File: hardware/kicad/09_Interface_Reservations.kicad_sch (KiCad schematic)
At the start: 27 parts

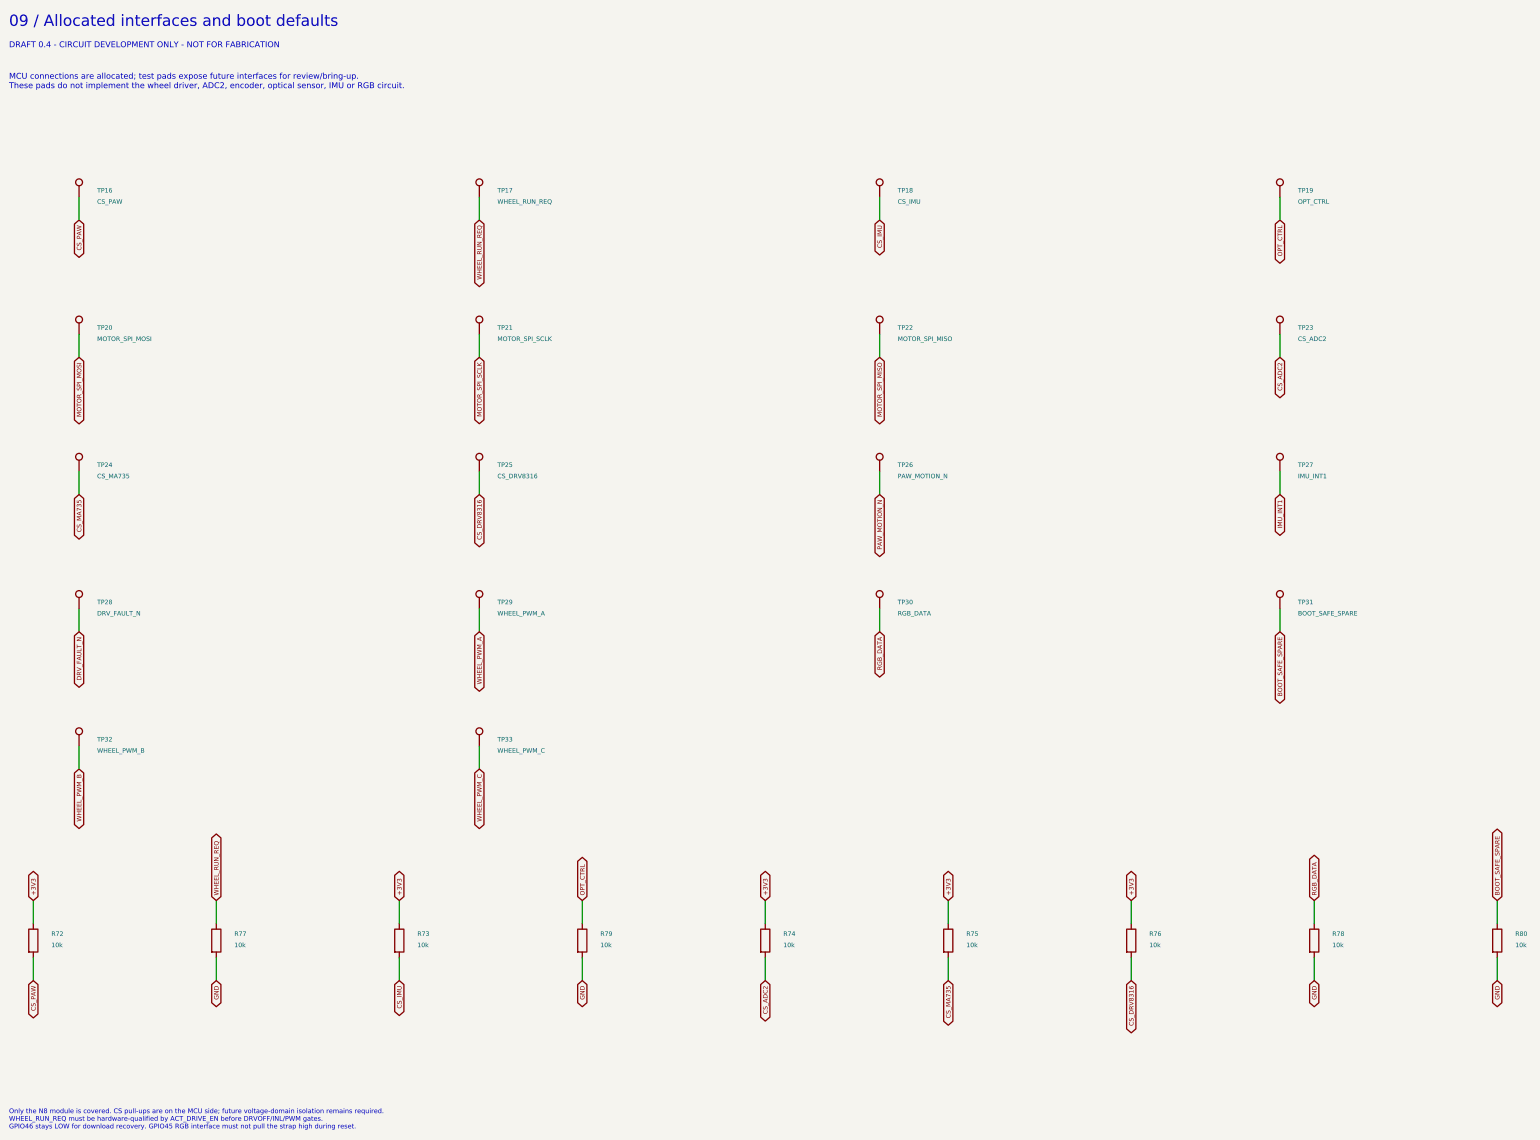
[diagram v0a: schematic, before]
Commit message: Add wheel control circuitry and autonomous regeneration brake
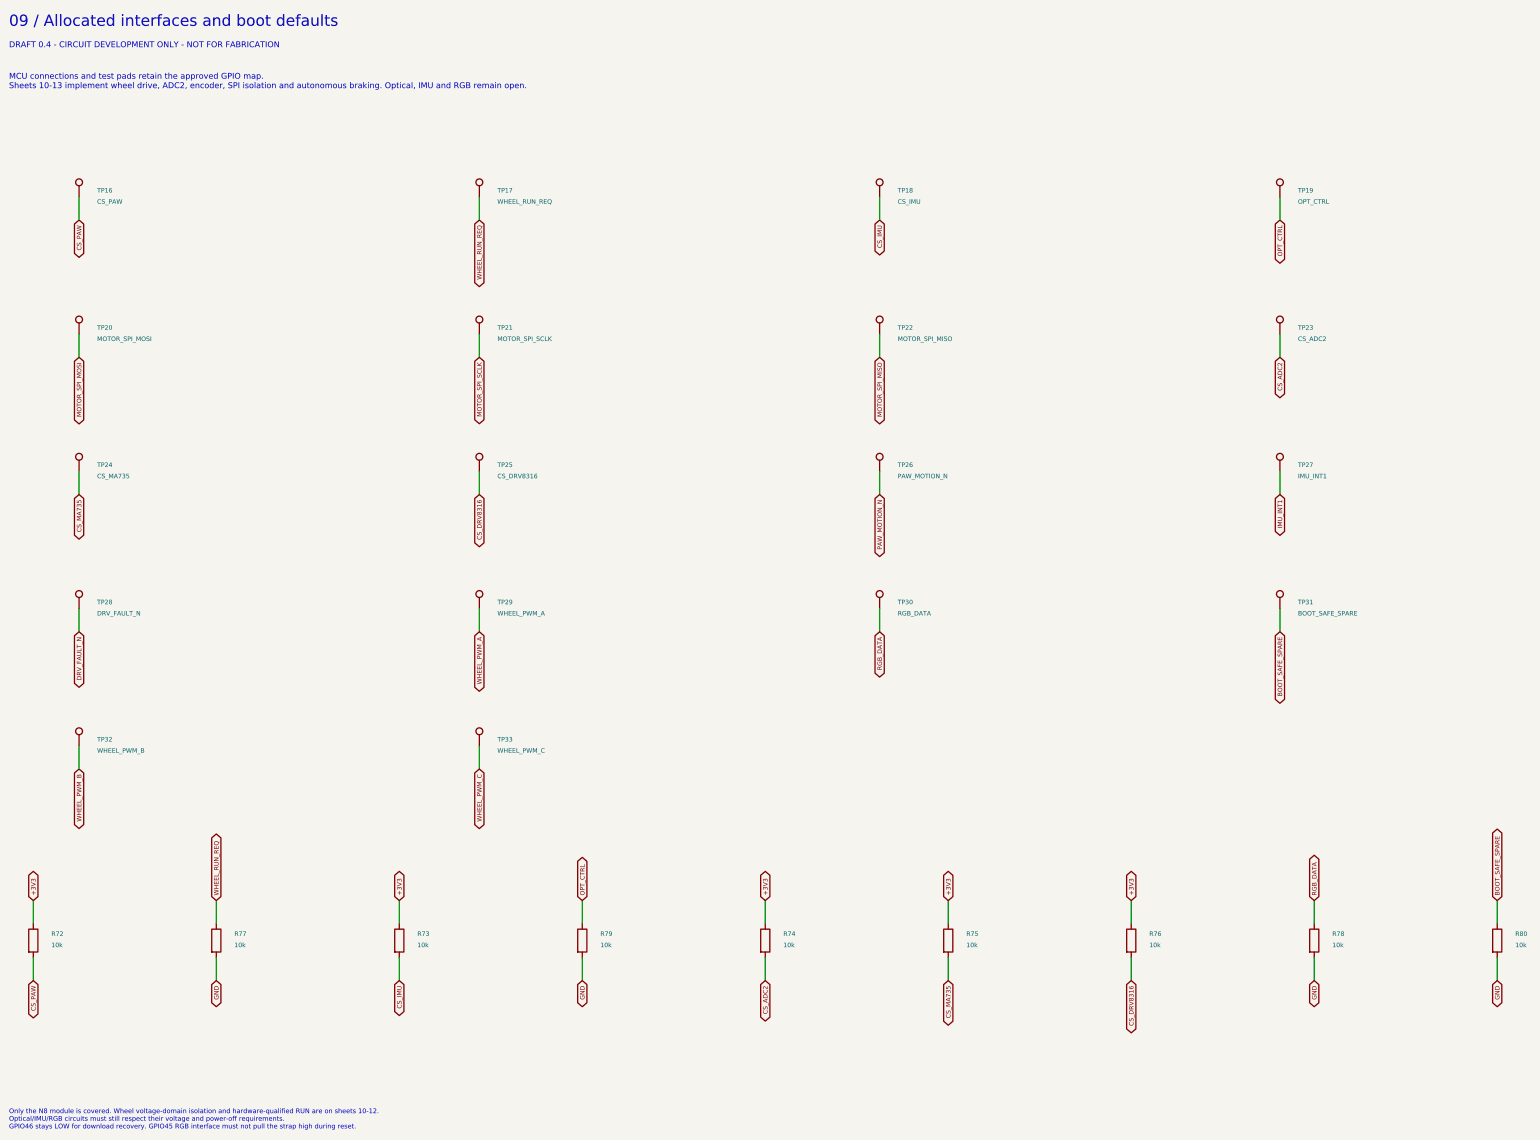
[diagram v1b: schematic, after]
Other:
- note added: "MCU connections and test pads retain the approved GPIO map. Sheets 10-13 implement wheel drive, ADC2, encoder, SPI isolation and autonomous braking. Optical, IMU and RGB remain open."
- note added: "Only the N8 module is covered. Wheel voltage-domain isolation and hardware-qualified RUN are on sheets 10-12. Optical/IMU/RGB circuits must still respect their voltage and power-off requirements. GPIO46 stays LOW for download recovery. GPIO45 RGB interface must not pull the strap high during reset."
- note removed: "MCU connections are allocated; test pads expose future interfaces for review/bring-up. These pads do not implement the wheel driver, ADC2, encoder, optical sensor, IMU or RGB circuit."
- note removed: "Only the N8 module is covered. CS pull-ups are on the MCU side; future voltage-domain isolation remains required. WHEEL_RUN_REQ must be hardware-qualified by ACT_DRIVE_EN before DRVOFF/INL/PWM gates. GPIO46 stays LOW for download recovery. GPIO45 RGB interface must not pull the strap high during reset."
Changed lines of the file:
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@@
       (justify left top))
 )
-  (text "MCU connections are allocated; test pads expose future interfaces for review/bring-up.\nThese pads do not implement the wheel driver, ADC2, encoder, optical sensor, IMU or RGB circuit."
+  (text "MCU connections and test pads retain the approved GPIO map.\nSheets 10-13 implement wheel drive, ADC2, encoder, SPI isolation and autonomous braking. Optical, IMU and RGB remain open."
     (at 20 31 0)
     (effects
@@
       (justify right))
 )
-  (text "Only the N8 module is covered. CS pull-ups are on the MCU side; future voltage-domain isolation remains required.\nWHEEL_RUN_REQ must be hardware-qualified by ACT_DRIVE_EN before DRVOFF/INL/PWM gates.\nGPIO46 stays LOW for download recovery. GPIO45 RGB interface must not pull the strap high during reset."
+  (text "Only the N8 module is covered. Wheel voltage-domain isolation and hardware-qualified RUN are on sheets 10-12.\nOptical/IMU/RGB circuits must still respect their voltage and power-off requirements.\nGPIO46 stays LOW for download recovery. GPIO45 RGB interface must not pull the strap high during reset."
     (at 20 261 0)
     (effects
